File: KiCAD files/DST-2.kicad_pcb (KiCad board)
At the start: 2 copper layers, 99 x 99 mm, 204 parts, among them J1 Barrel_Jack_MountingPin, J2 FTSW, J3 Power, J4 Pot_Dis, J5 Pot_Tone, J6 Pot_Vol, Q1 2N3904, Q2 2N3904, Q3 2N3904, U1 TL072

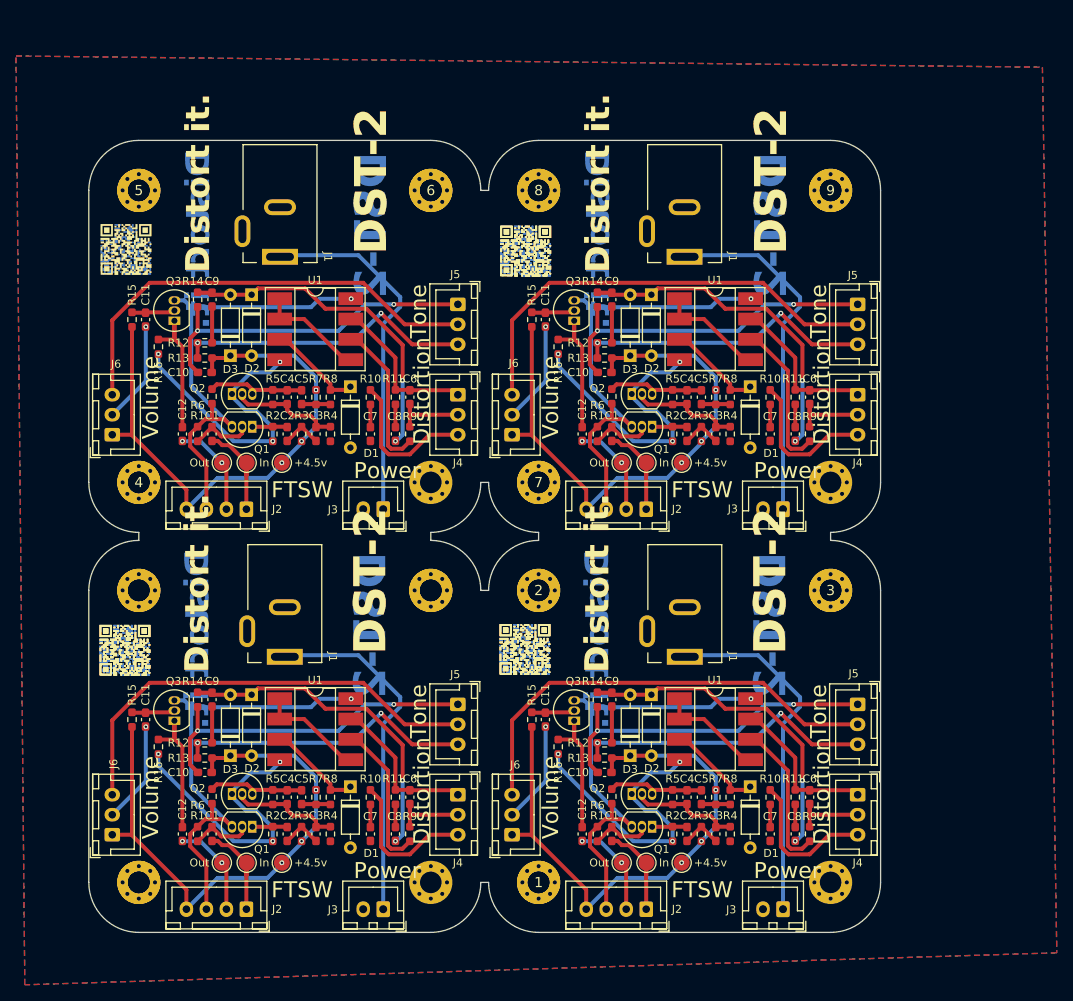
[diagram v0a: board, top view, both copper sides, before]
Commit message: Modified schematic and started a new PCB design
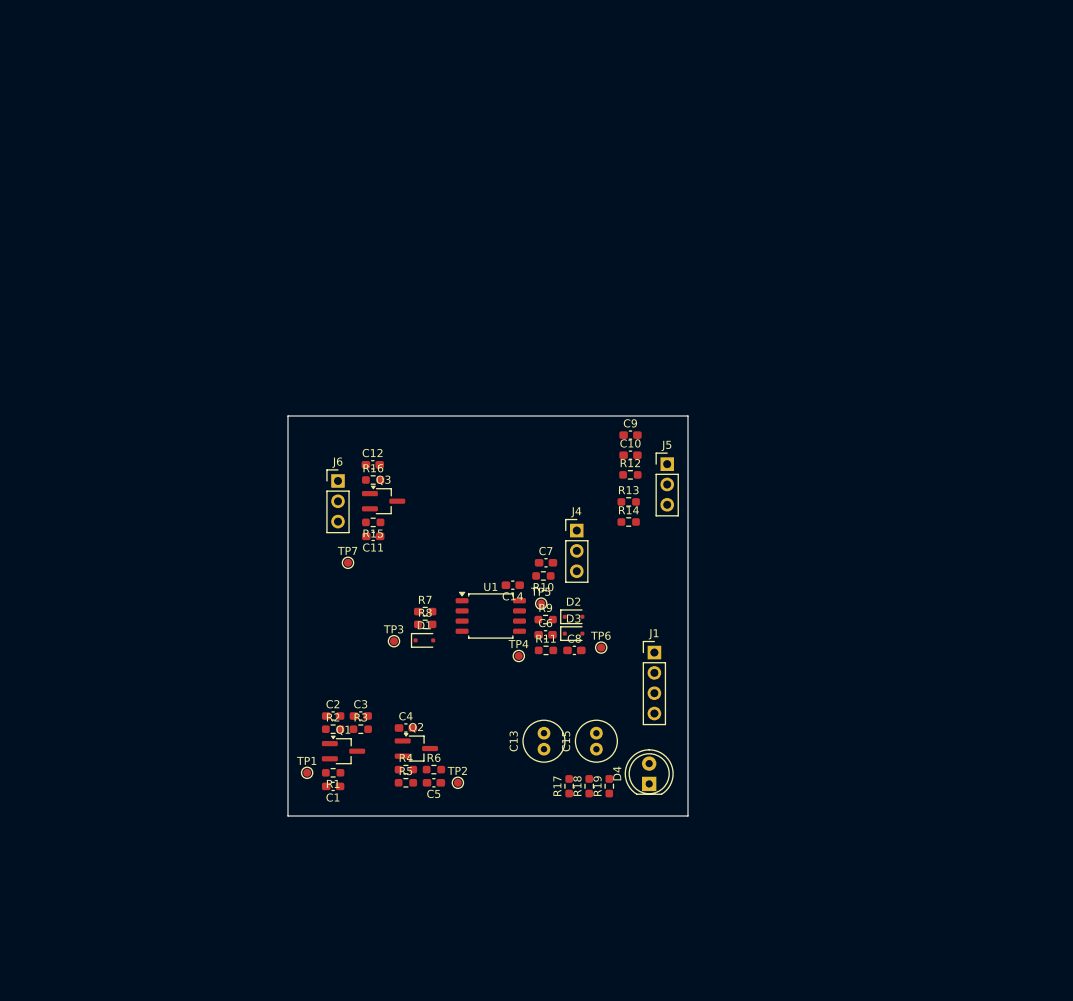
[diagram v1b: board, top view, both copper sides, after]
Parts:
- removed +4.5v (x4), In (x4), Out (x4): TestPoint_Pad_D2.0mm, TestPoint:TestPoint_Pad_D2.0mm
- removed 1, 2, 3, 4, 5, 6, 7, 8, 9, ? (x3): , 
- removed the C1 at (165.5, 127.2)
- removed the C1 at (115.5, 77.2)
- removed the C1 at (165.5, 77.2)
- removed the C1 at (115.5, 127.2)
- removed the C10 at (114.6, 69.5)
- removed the C10 at (114.6, 119.5)
- removed the C10 at (164.6, 69.5)
- removed the C10 at (164.6, 119.5)
- removed the C11 at (157.2, 113.0)
- removed the C11 at (107.2, 113.0)
- removed the C11 at (157.2, 63.0)
- removed the C11 at (107.2, 63.0)
- removed the C12 at (161.8, 77.2)
- removed the C12 at (111.8, 127.2)
- removed the C12 at (161.8, 127.2)
- removed the C12 at (111.8, 77.2)
- removed the C2 at (124.9, 77.2)
- removed the C2 at (174.9, 77.2)
- removed the C2 at (174.9, 127.2)
- removed the C2 at (124.9, 127.2)
- removed the C3 at (178.5, 127.2)
- removed the C3 at (128.5, 127.2)
- removed the C3 at (128.5, 77.2)
- removed the C3 at (178.5, 77.2)
- removed the C4 at (174.9, 122.7)
- removed the C4 at (174.9, 72.7)
- removed the C4 at (124.9, 122.7)
- removed the C4 at (124.9, 72.7)
- removed the C5 at (126.7, 72.7)
- removed the C5 at (176.7, 122.7)
- removed the C5 at (176.7, 72.7)
- removed the C5 at (126.7, 122.7)
- removed the C6 at (140.2, 122.6)
- removed the C6 at (190.2, 72.6)
- removed the C6 at (190.2, 122.6)
- removed the C6 at (140.2, 72.6)
- removed the C7 at (135.3, 127.2)
- removed the C7 at (185.3, 77.2)
- removed the C7 at (135.3, 77.2)
- removed the C7 at (185.3, 127.2)
- removed the C8 at (188.4, 127.2)
- removed the C8 at (138.4, 77.2)
- removed the C8 at (188.4, 77.2)
- removed the C8 at (138.4, 127.2)
- removed the C9 at (165.5, 110.5)
- removed the C9 at (165.5, 60.5)
- removed the C9 at (115.5, 110.5)
- removed the C9 at (115.5, 60.5)
- removed the D1 at (182.8, 121.3)
- removed the D1 at (182.8, 71.3)
- removed the D1 at (132.8, 71.3)
- removed the D1 at (132.8, 121.3)
- removed the D2 at (170.4, 59.8)
- removed the D2 at (120.5, 59.8)
- removed the D2 at (120.5, 109.8)
- removed the D2 at (170.4, 109.8)
- removed the D3 at (167.8, 117.5)
- removed the D3 at (117.8, 117.5)
- removed the D3 at (167.8, 67.5)
- removed the D3 at (117.8, 67.5)
- removed the J1 at (124.0, 55.1)
- removed the J1 at (174.6, 105.1)
- removed the J1 at (174.6, 55.1)
- removed the J1 at (124.6, 105.1)
- removed J2 (x4): FTSW, Connector_JST:JST_XH_B4B-XH-A_1x04_P2.50mm_Vertical
- removed J3 (x4): Power, Connector_JST:JST_XH_B2B-XH-A_1x02_P2.50mm_Vertical
- removed the J4 at (146.2, 72.3)
- removed the J4 at (196.2, 72.3)
- removed the J4 at (196.2, 122.3)
- removed the J4 at (146.2, 122.3)
- removed the J5 at (196.2, 61.0)
- removed the J5 at (146.2, 61.0)
- removed the J5 at (146.2, 111.0)
- removed the J5 at (196.2, 111.0)
- removed the J6 at (153.0, 77.3)
- removed the J6 at (103.0, 77.3)
- removed the J6 at (153.0, 127.3)
- removed the J6 at (103.0, 127.3)
- removed the Q1 at (120.5, 126.3)
- removed the Q1 at (170.5, 76.3)
- removed the Q1 at (170.5, 126.3)
- removed the Q1 at (120.5, 76.3)
- removed the Q2 at (118.0, 122.2)
- removed the Q2 at (118.0, 72.2)
- removed the Q2 at (168.0, 122.2)
- removed the Q2 at (168.0, 72.2)
- removed the Q3 at (110.8, 113.1)
- removed the Q3 at (110.8, 63.1)
- removed the Q3 at (160.8, 63.1)
- removed the Q3 at (160.8, 113.1)
- removed the R1 at (113.7, 127.2)
- removed the R1 at (163.7, 77.2)
- removed the R1 at (163.7, 127.2)
- removed the R1 at (113.7, 77.2)
- removed the R10 at (185.3, 72.7)
- removed the R10 at (185.3, 122.7)
- removed the R10 at (135.3, 122.7)
- removed the R10 at (135.3, 72.7)
- removed the R11 at (188.4, 122.6)
- removed the R11 at (188.4, 72.6)
- removed the R11 at (138.4, 122.6)
- removed the R11 at (138.4, 72.6)
- removed the R12 at (164.6, 115.8)
- removed the R12 at (164.6, 65.8)
- removed the R12 at (114.6, 115.8)
- removed the R12 at (114.6, 65.8)
- removed the R13 at (114.6, 117.8)
- removed the R13 at (164.6, 67.8)
- removed the R13 at (114.6, 67.8)
- removed the R13 at (164.6, 117.8)
- removed the R14 at (163.7, 60.5)
- removed the R14 at (113.7, 110.5)
- removed the R14 at (163.7, 110.5)
- removed the R14 at (113.7, 60.5)
- removed the R15 at (105.5, 63.0)
- removed the R15 at (155.5, 63.0)
- removed the R15 at (105.5, 113.0)
- removed the R15 at (155.5, 113.0)
- removed the R16 at (158.8, 116.3)
- removed the R16 at (158.8, 66.3)
- removed the R16 at (108.8, 116.3)
- removed the R16 at (108.8, 66.3)
- removed the R2 at (123.1, 77.2)
- removed the R2 at (173.1, 127.2)
- removed the R2 at (123.1, 127.2)
- removed the R2 at (173.1, 77.2)
- removed the R3 at (126.7, 77.2)
- removed the R3 at (176.7, 77.2)
- removed the R3 at (176.7, 127.2)
- removed the R3 at (126.7, 127.2)
- removed the R4 at (180.3, 77.2)
- removed the R4 at (180.3, 127.2)
- removed the R4 at (130.3, 77.2)
- removed the R4 at (130.3, 127.2)
- removed the R5 at (123.1, 122.7)
- removed the R5 at (173.1, 122.7)
- removed the R5 at (173.1, 72.7)
- removed the R5 at (123.1, 72.7)
- removed the R6 at (165.5, 72.5)
- removed the R6 at (115.5, 122.5)
- removed the R6 at (165.5, 122.5)
- removed the R6 at (115.5, 72.5)
- removed the R7 at (128.5, 122.7)
- removed the R7 at (178.5, 72.7)
- removed the R7 at (128.5, 72.7)
- removed the R7 at (178.5, 122.7)
- removed the R8 at (180.3, 72.7)
- removed the R8 at (130.3, 122.7)
- removed the R8 at (180.3, 122.7)
- removed the R8 at (130.3, 72.7)
- removed the R9 at (140.2, 127.2)
- removed the R9 at (140.2, 77.2)
- removed the R9 at (190.2, 77.2)
- removed the R9 at (190.2, 127.2)
- removed REF** (x4), REF**1, REF**10, REF**11, REF**12, REF**2, REF**3, REF**4, REF**5, REF**6, REF**7, REF**8, REF**9: MountingHole_2.7mm_M2.5_Pad_Via, MountingHole:MountingHole_2.7mm_M2.5_Pad_Via
- removed the U1 at (128.4, 64.2)
- removed the U1 at (178.4, 64.2)
- removed the U1 at (178.4, 114.2)
- removed the U1 at (128.4, 114.2)
- added C1: 47nF, Capacitor_SMD:C_0603_1608Metric_Pad1.08x0.95mm_HandSolder, F.Cu at (130.6, 121.3)
- added C10: 10nF, Capacitor_SMD:C_0603_1608Metric_Pad1.08x0.95mm_HandSolder, F.Cu at (167.8, 79.9)
- added C11: 47nF, Capacitor_SMD:C_0603_1608Metric_Pad1.08x0.95mm_HandSolder, F.Cu at (135.7, 90.0)
- added C12: 1µF, Capacitor_SMD:C_0603_1608Metric_Pad1.08x0.95mm_HandSolder, F.Cu at (135.6, 81.1)
- added C13: 10µF, Capacitor_THT:C_Radial_D5.0mm_H11.0mm_P2.00mm, F.Cu at (157.0, 116.7)
- added C14: 100nF, Capacitor_SMD:C_0603_1608Metric_Pad1.08x0.95mm_HandSolder, F.Cu at (153.1, 96.2)
- added C15: 47uF, Capacitor_THT:C_Radial_D5.0mm_H11.0mm_P2.00mm, F.Cu at (163.6, 116.7)
- added C2: 470nF, Capacitor_SMD:C_0603_1608Metric_Pad1.08x0.95mm_HandSolder, F.Cu at (130.6, 112.5)
- added C3: 47nF, Capacitor_SMD:C_0603_1608Metric_Pad1.08x0.95mm_HandSolder, F.Cu at (134.1, 112.5)
- added C4: 250pF, Capacitor_SMD:C_0603_1608Metric_Pad1.08x0.95mm_HandSolder, F.Cu at (139.7, 114.0)
- added C5: 68nF, Capacitor_SMD:C_0603_1608Metric_Pad1.08x0.95mm_HandSolder, F.Cu at (143.2, 120.8)
- added C6: 100pF, Capacitor_SMD:C_0603_1608Metric_Pad1.08x0.95mm_HandSolder, F.Cu at (157.2, 102.3)
- added C7: 470nF, Capacitor_SMD:C_0603_1608Metric_Pad1.08x0.95mm_HandSolder, F.Cu at (157.2, 93.3)
- added C8: 470nF, Capacitor_SMD:C_0603_1608Metric_Pad1.08x0.95mm_HandSolder, F.Cu at (160.8, 104.3)
- added C9: 22nF, Capacitor_SMD:C_0603_1608Metric_Pad1.08x0.95mm_HandSolder, F.Cu at (167.8, 77.4)
- added D1: 1N4148, Diode_SMD:D_SOD-323F, F.Cu at (142.1, 103.0)
- added D2: 1N4148, Diode_SMD:D_SOD-323F, F.Cu at (160.7, 100.1)
- added D3: 1N4148, Diode_SMD:D_SOD-323F, F.Cu at (160.7, 102.2)
- added D4: LED, LED_THT:LED_D5.0mm, F.Cu at (170.2, 121.0)
- added J1: FTSW, Connector_PinHeader_2.54mm:PinHeader_1x04_P2.54mm_Vertical, F.Cu at (170.8, 104.6)
- added J4: Pot_Dis, Connector_PinHeader_2.54mm:PinHeader_1x03_P2.54mm_Vertical, F.Cu at (161.1, 89.3)
- added J5: Pot_Tone, Connector_PinHeader_2.54mm:PinHeader_1x03_P2.54mm_Vertical, F.Cu at (172.4, 81.0)
- added J6: Pot_Vol, Connector_PinHeader_2.54mm:PinHeader_1x03_P2.54mm_Vertical, F.Cu at (131.2, 83.1)
- added Q1: 2N3904, Package_TO_SOT_SMD:TSOT-23_HandSoldering, F.Cu at (131.9, 116.9)
- added Q2: 2N3904, Package_TO_SOT_SMD:TSOT-23_HandSoldering, F.Cu at (141.0, 116.6)
- added Q3: 2N3904, Package_TO_SOT_SMD:TSOT-23_HandSoldering, F.Cu at (136.9, 85.7)
- added R1: 470kΩ, Resistor_SMD:R_0603_1608Metric_Pad0.98x0.95mm_HandSolder, F.Cu at (130.6, 119.6)
- added R10: 4.7kΩ, Resistor_SMD:R_0603_1608Metric_Pad0.98x0.95mm_HandSolder, F.Cu at (156.9, 95.0)
- added R11: 2.2kΩ, Resistor_SMD:R_0603_1608Metric_Pad0.98x0.95mm_HandSolder, F.Cu at (157.2, 104.3)
- added R12: 2.2kΩ, Resistor_SMD:R_0603_1608Metric_Pad0.98x0.95mm_HandSolder, F.Cu at (167.8, 82.4)
- added R13: 6.8kΩ, Resistor_SMD:R_0603_1608Metric_Pad0.98x0.95mm_HandSolder, F.Cu at (167.6, 85.7)
- added R14: 6.8kΩ, Resistor_SMD:R_0603_1608Metric_Pad0.98x0.95mm_HandSolder, F.Cu at (167.6, 88.2)
- added R15: 1MΩ, Resistor_SMD:R_0603_1608Metric_Pad0.98x0.95mm_HandSolder, F.Cu at (135.7, 88.3)
- added R16: 10kΩ, Resistor_SMD:R_0603_1608Metric_Pad0.98x0.95mm_HandSolder, F.Cu at (135.7, 83.0)
- added R17: 10k, Resistor_SMD:R_0603_1608Metric_Pad0.98x0.95mm_HandSolder, F.Cu at (160.1, 121.3)
- added R18: 10k, Resistor_SMD:R_0603_1608Metric_Pad0.98x0.95mm_HandSolder, F.Cu at (162.7, 121.3)
- added R19: 1k, Resistor_SMD:R_0603_1608Metric_Pad0.98x0.95mm_HandSolder, F.Cu at (165.2, 121.3)
- added R2: 10kΩ, Resistor_SMD:R_0603_1608Metric_Pad0.98x0.95mm_HandSolder, F.Cu at (130.6, 114.2)
- added R3: 100kΩ, Resistor_SMD:R_0603_1608Metric_Pad0.98x0.95mm_HandSolder, F.Cu at (134.1, 114.2)
- added R4: 100kΩ, Resistor_SMD:R_0603_1608Metric_Pad0.98x0.95mm_HandSolder, F.Cu at (139.7, 119.2)
- added R5: 470kΩ, Resistor_SMD:R_0603_1608Metric_Pad0.98x0.95mm_HandSolder, F.Cu at (139.7, 120.8)
- added R6: 10kΩ, Resistor_SMD:R_0603_1608Metric_Pad0.98x0.95mm_HandSolder, F.Cu at (143.2, 119.2)
- added R7: 100kΩ, Resistor_SMD:R_0603_1608Metric_Pad0.98x0.95mm_HandSolder, F.Cu at (142.2, 99.5)
- added R8: 47kΩ, Resistor_SMD:R_0603_1608Metric_Pad0.98x0.95mm_HandSolder, F.Cu at (142.2, 101.0)
- added R9: 100kΩ, Resistor_SMD:R_0603_1608Metric_Pad0.98x0.95mm_HandSolder, F.Cu at (157.2, 100.5)
- added TP1: INPUT, TestPoint:TestPoint_Pad_D1.0mm, F.Cu at (127.4, 119.6)
- added TP2: Q2 COLLECTOR, TestPoint:TestPoint_Pad_D1.0mm, F.Cu at (146.2, 120.8)
- added TP3: OP1 IN, TestPoint:TestPoint_Pad_D1.0mm, F.Cu at (138.2, 103.2)
- added TP4: OP1 OUT, TestPoint:TestPoint_Pad_D1.0mm, F.Cu at (153.8, 105.0)
- added TP5: OP-AMP OUTPUT, TestPoint:TestPoint_Pad_D1.0mm, F.Cu at (156.7, 98.5)
- added TP6: CLIPPING, TestPoint:TestPoint_Pad_D1.0mm, F.Cu at (164.2, 104.0)
- added TP7: Q3 B, TestPoint:TestPoint_Pad_D1.0mm, F.Cu at (132.5, 93.3)
- added U1: TL072, Package_SO:SOIC-8_5.3x5.3mm_P1.27mm, F.Cu at (150.3, 100.0)
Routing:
- net +4,5v: track 284.4 -> 0.00 mm, vias 12 -> 0
- net +9V: track 235.6 -> 0.00 mm, vias 4 -> 0
- net Net-(J5-Pin_2): track 226.4 -> 0.00 mm
- net Vbatt: track 176.0 -> 0.00 mm
- net Net-(J5-Pin_1): track 171.6 -> 0.00 mm, vias 8 -> 0
- net Net-(D2-K): track 165.9 -> 0.00 mm, vias 8 -> 0
- net Net-(J5-Pin_3): track 150.4 -> 0.00 mm, vias 8 -> 0
- net GND: track 145.1 -> 0.00 mm, vias 12 -> 0
- net Net-(J4-Pin_1): track 78.9 -> 0.00 mm
- net Net-(U1B--): track 78.8 -> 0.00 mm
- net Net-(J4-Pin_3): track 75.1 -> 0.00 mm
- net Net-(Q3-E): track 72.2 -> 0.00 mm
- net Net-(Q2-B): track 55.2 -> 0.00 mm
- net Net-(U1A--): track 54.1 -> 0.00 mm
- net in_p: track 51.4 -> 0.00 mm
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- removed copper zone on B.Cu, net GND
- removed copper zone on F.Cu, net GND
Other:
- board size 99 x 99 mm -> 50 x 50 mm
- board text removed: "DST-2"
- board text removed: "Distort it."
- board text removed: "Distortion"
- board text removed: "FTSW"
- board text removed: "Power"
- board text removed: "Tone"
- board text removed: "Volume"

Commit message: Finished PCB design
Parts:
- moved J1 43.9 mm to (130.7, 122.5), turned to 90 degrees
- moved C9 41.8 mm to (144.0, 111.8), turned to -90 degrees
- moved R12 39.0 mm to (142.2, 111.8), turned to 90 degrees
- moved J6 38.4 mm to (156.8, 111.8), turned to 180 degrees
- moved C10 38.0 mm to (148.5, 112.7), turned to 180 degrees
- moved J5 36.6 mm to (152.7, 111.8), turned to 180 degrees
- moved R14 32.0 mm to (145.8, 111.8), turned to -90 degrees
- moved R13 31.5 mm to (148.5, 110.8)
- moved TP7 30.8 mm to (160.2, 106.8)
- moved R19 26.6 mm to (138.7, 118.7)
- moved C12 26.0 mm to (157.9, 94.3), turned to 90 degrees
- moved R18 25.8 mm to (136.9, 118.7)
- moved R17 25.1 mm to (135.2, 118.7), turned to -90 degrees
- moved C11 25.0 mm to (157.7, 101.8), turned to 90 degrees
- moved Q3 24.6 mm to (158.2, 98.1)
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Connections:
- C1 pad 1: in_p -> IN_P
- C12 pad 2: out_p -> OUT_P
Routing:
- net +9V: track 0.00 -> 97.2 mm, vias 0 -> 4
- net +4,5v: track 0.00 -> 82.0 mm, vias 0 -> 4
- net GND: track 0.00 -> 59.3 mm, vias 0 -> 8
- net OUT_P: track 0.00 -> 41.7 mm, vias 0 -> 1
- net Net-(D4-K): track 0.00 -> 23.3 mm
- net IN_P: track 0.00 -> 22.4 mm, vias 0 -> 1
- net Net-(J4-Pin_1): track 0.00 -> 14.7 mm
- net Net-(Q2-C): track 0.00 -> 13.4 mm, vias 0 -> 2
- net Net-(C5-Pad2): track 0.00 -> 12.8 mm, vias 0 -> 2
- net Net-(J5-Pin_3): track 0.00 -> 12.2 mm, vias 0 -> 2
- net Net-(U1A--): track 0.00 -> 12.0 mm
- net Net-(C8-Pad1): track 0.00 -> 11.8 mm, vias 0 -> 2
- net Net-(D1-K): track 0.00 -> 11.0 mm
- net Net-(Q3-B): track 0.00 -> 10.8 mm
- net Net-(D2-K): track 0.00 -> 10.7 mm
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- added copper zone on B.Cu, net GND
- added copper zone on F.Cu, net GND
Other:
- board size 50 x 50 mm -> 37.8 x 34.7 mm
